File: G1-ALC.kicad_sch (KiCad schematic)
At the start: 91 parts, among them J101 Conn_01x03_Pin, J102 330 VAC In, J103 G1 connections, J104 105VAC in, J105 Conn_01x03_Pin, J107 Conn_01x05_Pin, J108 G2 Control board interconnect, Q101 TIP122, U101 LM7812_TO220, U102 LM324, U103 MCT5211M, U301 CNY17-4

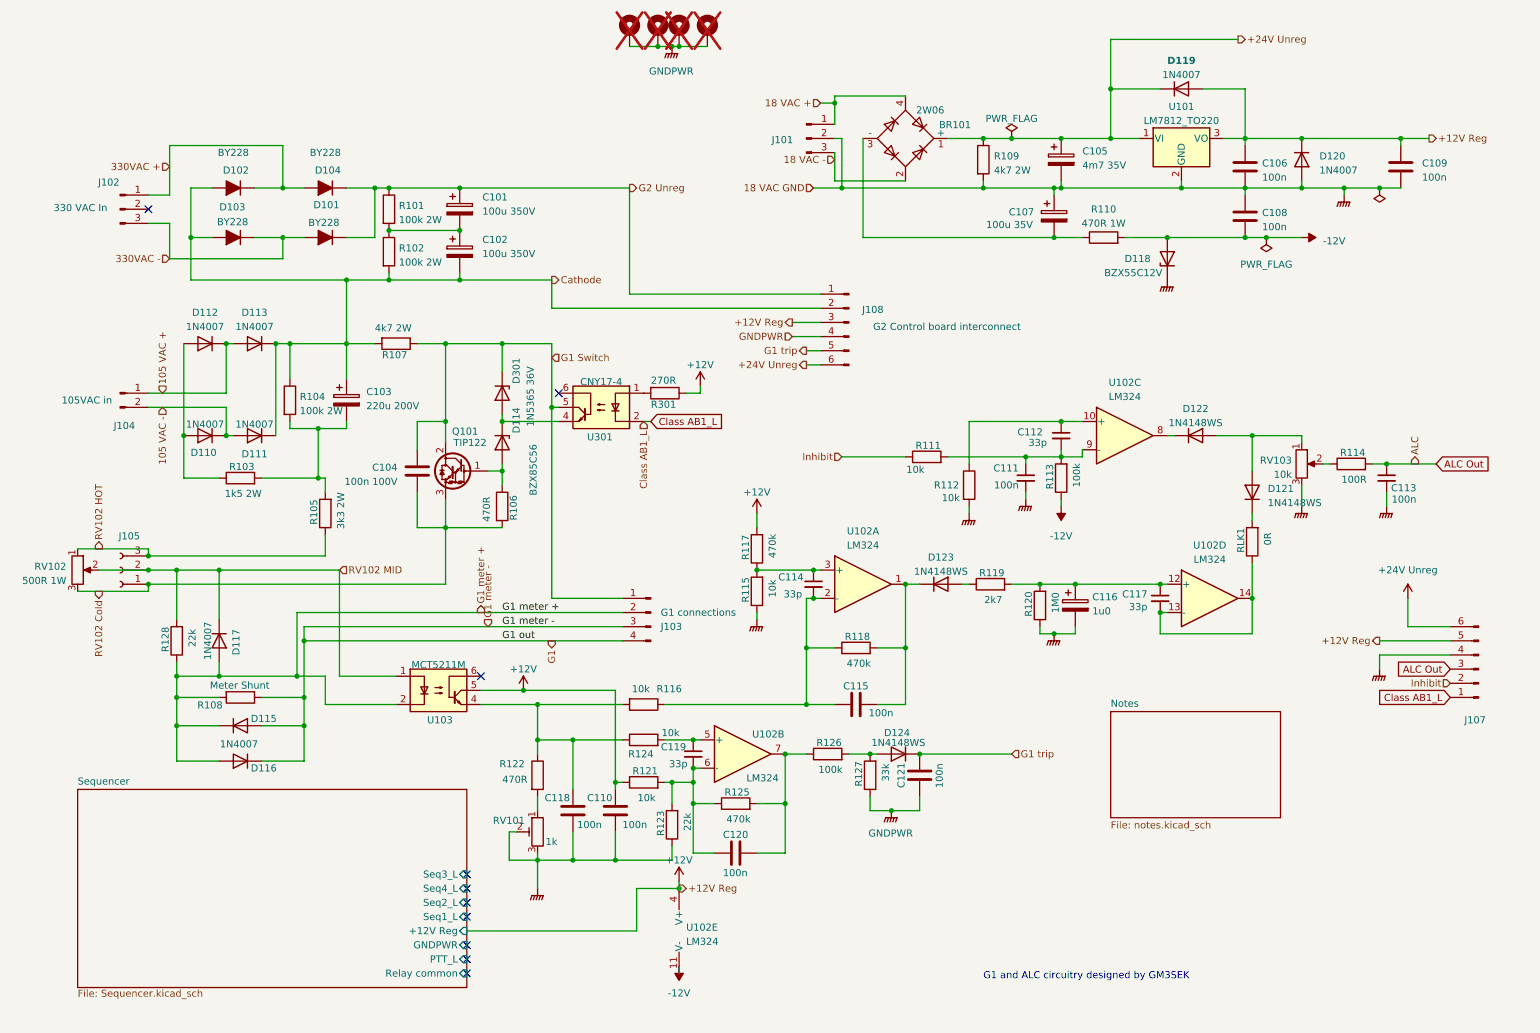
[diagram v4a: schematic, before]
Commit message: Cleanup schematic. No functional change.
Replaced global labels with hierarchical.
Consistent placement of references and values.
Values typed in a smaller font.
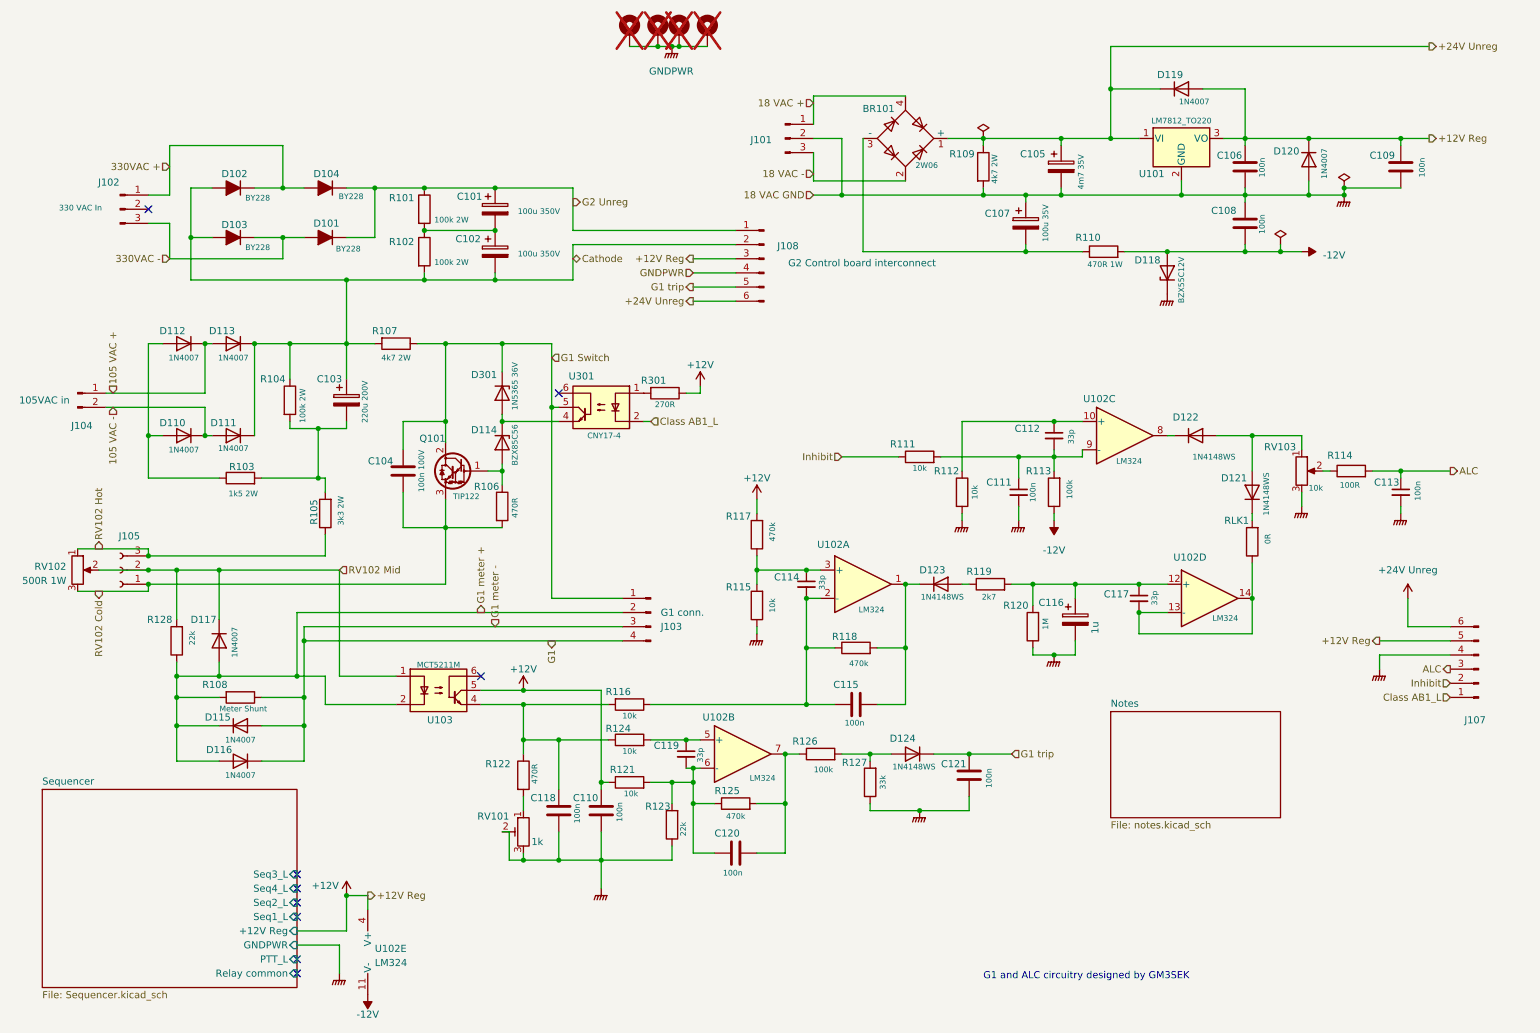
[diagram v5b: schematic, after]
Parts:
- C116: value 1u0 -> 1u
- J103: value G1 connections -> G1 conn.
- R120: value 1M0 -> 1M
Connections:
- net ALC Out renamed ALC
- net RV102 HOT renamed RV102 Hot
- net RV102 MID renamed RV102 Mid
- no-connect marks 10 -> 9
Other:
- moved on the sheet: C101, C102, C104, C105, C107, C108, C110, C111, C112, C113, C114, C116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

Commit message: Moved cold end of R115 to CLASS_AB1_L instead of GND. The intent is to turn off ALC in case we want to run the PA in class C.
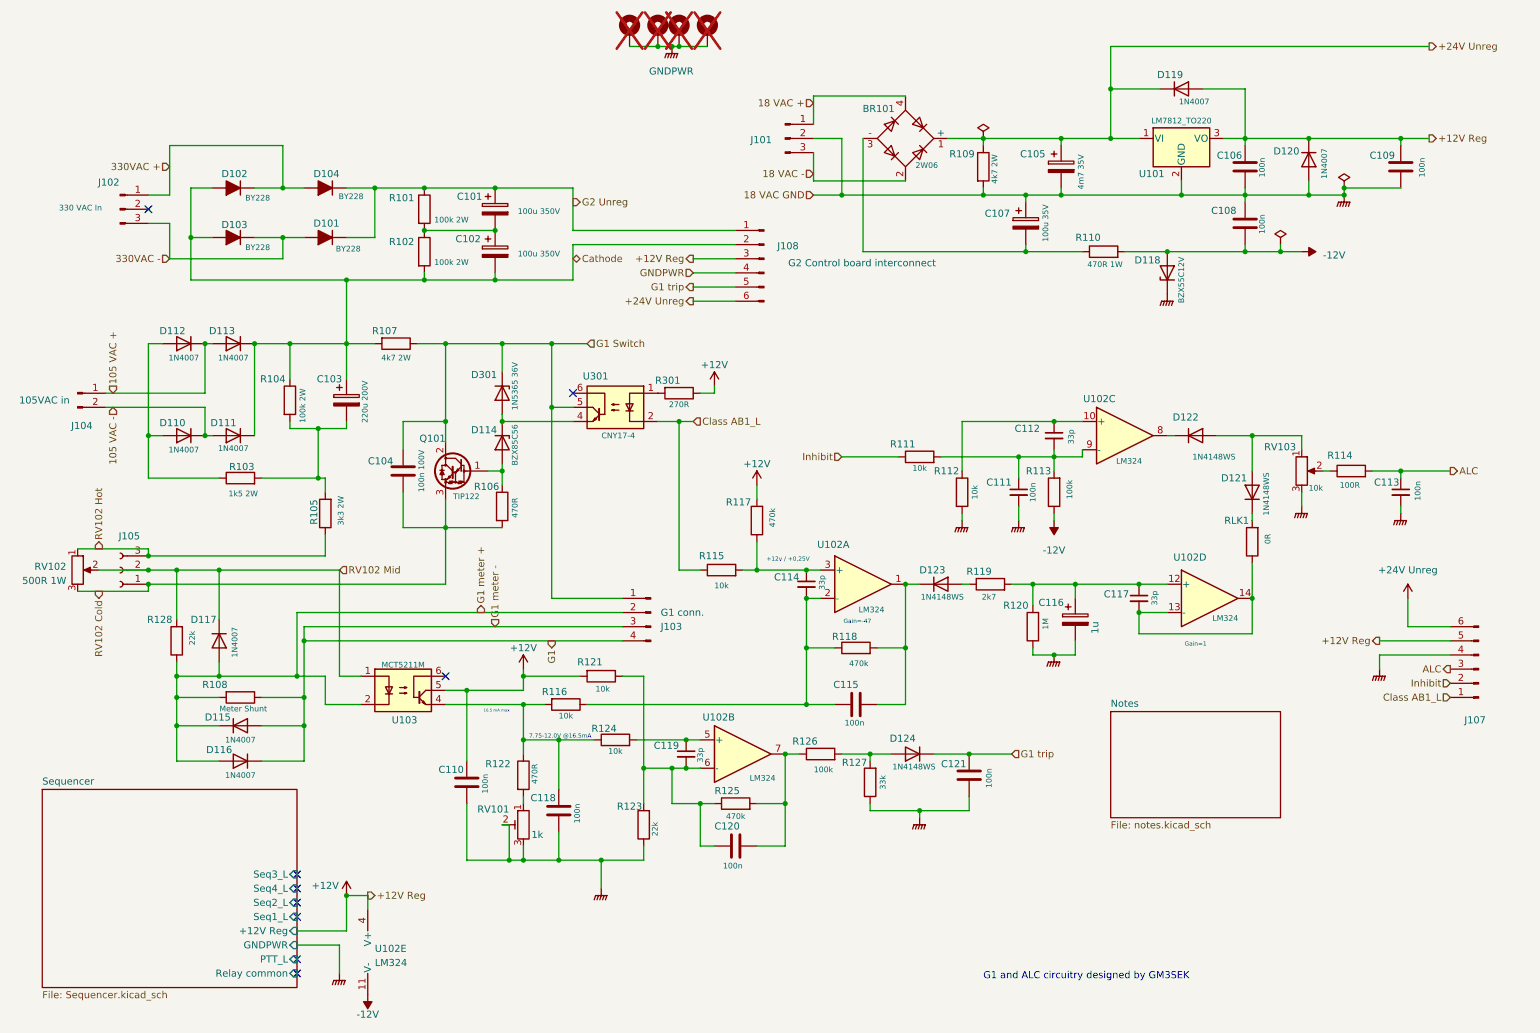
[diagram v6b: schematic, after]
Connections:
- net +12V: now also R121.2; no longer R121.1
- net Class AB1_L: now also R115.1
- net GNDPWR: no longer R115.1
- net at C119.2, C120.1, R123.2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: now also R121.1; no longer R121.2
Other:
- note added: "+12v / +0,25V"
- note added: "16.5 mA max"
- note added: "7.75-12.0V @16.5mA"
- note added: "Gain=-47"
- note added: "Gain=1"
- moved on the sheet: C110, C120, R115, R116, R117, R121, R123, R124, R301, RV101, U103, U301

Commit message: Updated format to KiCad 9. Included footprints etc.
Standardized PCB layers, updated property formatting, and adjusted net assignments. Added some DigiKey, Electrokit, and Mouser component part numbers.
Reduced font sizes for better readability and incorporated embedded font settings.
Removed the sequencer from the schematic which wasn't really meant to be there.
Revised and excluded drc and erc warnings and exclusions.
Included footprints into the project library that formerly was defined outside of the project.
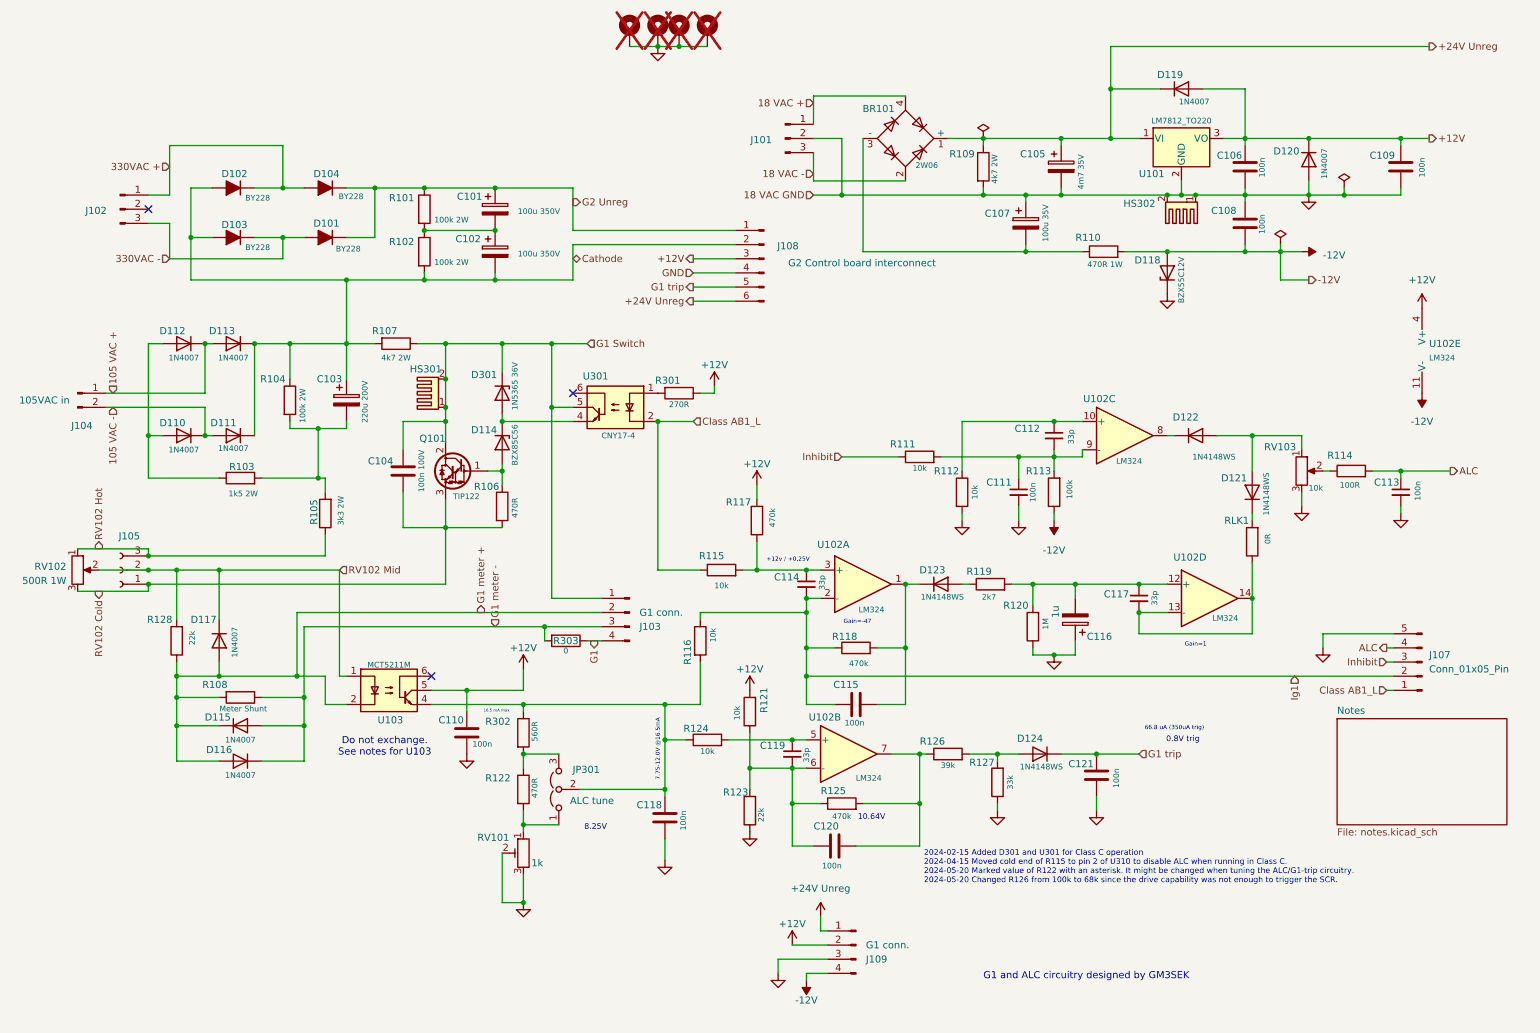
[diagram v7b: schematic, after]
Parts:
- removed J107: Conn_01x05_Pin, Connector_Phoenix_MSTB:PhoenixContact_MSTBVA_2,5_6-G-5,08_1x06_P5.08mm_Vertical, symbol Connector:Conn_01x06_Pin
- removed unit 5 of U102
- added HS301, HS302: Heatsink_Pad_2Pin, Project_library:6025DG_Cooler, symbol Mechanical:Heatsink_Pad_2Pin
- added J107: Conn_01x05_Pin, Connector_Phoenix_MSTB:PhoenixContact_MSTBVA_2,5_5-G-5,08_1x05_P5.08mm_Vertical, symbol Connector:Conn_01x05_Pin
- added J109: G1 conn., Connector_Phoenix_MSTB:PhoenixContact_MSTBVA_2,5_4-G-5,08_1x04_P5.08mm_Vertical, symbol Connector:Conn_01x04_Pin
- added JP301: ALC tune, Connector_PinHeader_2.54mm:PinHeader_1x03_P2.54mm_Vertical, symbol Jumper:Jumper_3_Open
- added R302: 560R, Resistor_SMD:R_1206_3216Metric, symbol Device:R
- added R303: 0, Jumper:SolderJumper-2_P1.3mm_Bridged2Bar_RoundedPad1.0x1.5mm, symbol Device:R
- BR101: Electrokit # (none) -> 40310051; Order # 40310051 -> (none); Supplier Electrokit -> (none)
- C101, C102: Electrokit # (none) -> 41004525; Order # 41004525 -> (none); Supplier Electrokit -> (none)
- C103: Electrokit # (none) -> 41019009; Order # 41019009 -> (none); Supplier Electrokit -> (none)
- C104: Electrokit # (none) -> 41015673; Order # 41015673 -> (none); Supplier Electrokit -> (none)
- C105: Electrokit # (none) -> 41016024; Order # 41016024 -> (none); Supplier Electrokit -> (none)
- C106, C108, C109, C110, C111, C113, C115, C118, C120, C121: Electrokit # (none) -> 40503054; Mouser # (none) -> 80-C1206C104M5R; Order # 40503054 -> (none); Supplier Electrokit -> (none)
- C107: Electrokit # (none) -> 41019011; Order # 41019011 -> (none); Supplier Electrokit -> (none)
- C112, C114, C117, C119: Electrokit # (none) -> 40502045; Mouser # (none) -> 791-0805N330K250CT; Order # 40502045 -> (none); Supplier Electrokit -> (none)
- C116: Electrokit # (none) -> 40503060; Mouser # (none) -> 187-CL31B105KAHNFNE; Order # 40503060 -> (none); Supplier Electrokit -> (none)
- D101, D102, D103, D104: footprint Diode_THT_AKL:D_SOD-64_P15.24mm_big_holes_Horizontal -> Project_library:D_SOD-64_P15.24mm_big_holes_Horizontal; Electrokit # (none) -> 40311228; Order # 40311228 -> (none); Supplier Electrokit -> (none)
- D110, D111, D112, D113, D115, D116, D117, D119, D120: Electrokit # (none) -> 40310007; Order # 40310007 -> (none); Supplier Electrokit -> (none)
- D114, D301: Electrokit # (none) -> 41020328; Order # 41020328 -> (none); Supplier Electrokit -> (none)
- D118: Electrokit # (none) -> 40310033; Order # 40310033 -> (none); Supplier Electrokit -> (none)
- D121, D122, D123, D124: Electrokit # (none) -> 41011670; Mouser # (none) -> 637-1N4148WS; Order # 41011670 -> (none); Supplier Electrokit -> (none)
- H101: renamed from H105; Supplier Elecrow -> (none)
- H102: renamed from H101; Supplier Elecrow -> (none)
- H103: renamed from H102; Supplier Elecrow -> (none)
- H104: renamed from H103; Supplier Elecrow -> (none)
- J101, J105: Electrokit # (none) -> 40210022; Order # 40210022 -> (none); Supplier Electrokit -> (none)
- J102: value 330 VAC In -> 330VAC; Electrokit # (none) -> 40210022; Order # 40210022 -> (none); Supplier Electrokit -> (none)
- J103: Electrokit # (none) -> 41017486; Order # 41017486 -> (none); Supplier Electrokit -> (none)
- J104: Electrokit # (none) -> 40210021; Order # 40210021 -> (none); Supplier Electrokit -> (none)
- J108: Electrokit # (none) -> 41017488; Order # 41017488 -> (none); Supplier Electrokit -> (none)
- Q101: footprint Package_TO_SOT_THT:TO-220-3_Vertical_Cooler -> Package_TO_SOT_THT:TO-220-3_Vertical; Electrokit # (none) -> 40320122; Order # 40320122 -> (none); Supplier Electrokit -> (none)
- R101, R102, R104: Electrokit # (none) -> 41011683; Order # 41011683 -> (none); Supplier Electrokit -> (none)
- R103: Electrokit # (none) -> 41011674; Order # 41011674 -> (none); Supplier Electrokit -> (none)
- R105: Electrokit # (none) -> 41011677; Order # 41011677 -> (none); Supplier Electrokit -> (none)
- R106: Electrokit # (none) -> 40818247; Mouser # (none) -> 603-AF1206JR-07470RL; Order # 40818247 -> (none); Supplier Electrokit -> (none)
- R107, R109: Electrokit # (none) -> 41011678; Order # 41011678 -> (none); Supplier Electrokit -> (none)
- R108: Electrokit # (none) -> 40818315; Order # 40818315 -> (none); Supplier Electrokit -> (none)
- R110: Electrokit # (none) -> 40812020; Order # 40812020 -> (none); Supplier Electrokit -> (none)
- R111, R112, R115, R116, R121, R124: Electrokit # (none) -> 40818410; Mouser # (none) -> 603-AC1206FR-0710KL; Order # 40818410 -> (none); Supplier Electrokit -> (none)
- R113: Electrokit # (none) -> 40818510; Mouser # (none) -> 708-RMCF1206JG100K; Order # 40818510 -> (none); Supplier Electrokit -> (none)
- R114: Electrokit # (none) -> 40818210; Mouser # (none) -> 603-RC1206JR-13100RL; Order # 40818210 -> (none); Supplier Electrokit -> (none)
- R117, R118, R125: Electrokit # (none) -> 40818547; Mouser # (none) -> 652-CR1206JW-474ELF; Order # 40818547 -> (none); Supplier Electrokit -> (none)
- R119: Electrokit # (none) -> 40818327; Mouser # (none) -> 652-CR1206FX-2701ELF; Order # 40818327 -> (none); Supplier Electrokit -> (none)
- R120: Electrokit # (none) -> 40818610; Mouser # (none) -> 279-CRGP1206F1M0; Order # 40818610 -> (none); Supplier Electrokit -> (none)
- R122: Order # 40818247 -> (none); Supplier Electrokit -> (none)
- R123, R128: Electrokit # (none) -> 40818315; Mouser # (none) -> 71-CRCW1206-22K-E3; Order # 40818315 -> (none); Supplier Electrokit -> (none)
- R126: value 100k -> 39k; Electrokit # (none) -> 40818510; Mouser # (none) -> 667-ERJ-P08J683V; Order # 40818510 -> (none); Supplier Electrokit -> (none)
- R127: Electrokit # (none) -> 40818433; Mouser # (none) -> 652-CR1206FX-3302ELF; Order # 40818433 -> (none); Supplier Electrokit -> (none)
- R301: Electrokit # (none) -> 40818227; Order # 40818227 -> (none); Supplier Electrokit -> (none)
- RLK1: Electrokit # (none) -> 40818433; Order # 40818433 -> (none); Supplier Electrokit -> (none)
- RV101: Electrokit # (none) -> 33860102; Order # 33860102 -> (none); Supplier Electrokit -> (none)
- RV102: Mouser # (none) -> 3109605596; Order # 3109605596 -> (none); Supplier Mouser -> (none)
- RV103: Electrokit # (none) -> 33860103; Order # 33860103 -> (none); Supplier Electrokit -> (none)
- U101: footprint Package_TO_SOT_THT:TO-220-3_Vertical_Cooler -> Package_TO_SOT_THT:TO-220-3_Vertical; Electrokit # (none) -> 41009663; Order # 41009663 -> (none); Supplier Electrokit -> (none)
- U102: Electrokit # (none) -> 40350324; Mouser # (none) -> 863-LM324DR2G; Order # 40350324 -> (none); Supplier Electrokit -> (none)
- U103: DigiKey # (none) -> MCT5211M-ND; Notes This component is crucial. It cannot simply be exchanged for any other optocoupler because its sensititity to low LED current is needed. -> This component is crucial. It cannot simply be exchanged for any other optocoupler because its sensititity to low grid current is needed.; Order # MCT5211M-ND -> (none); Supplier DigiKey -> (none)
- U301: DigiKey # (none) -> 751-1268-5-ND; Order # 751-1268-5-ND -> (none); Supplier DigiKey -> (none)
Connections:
- net +12V: now also U102.4 (V+), J109.2 (Pin_2)
- net +24V Unreg: now also J109.1 (Pin_1)
- net -12V: now also U102.11 (V-), J109.4 (Pin_4)
- net ALC: now also J107.4 (Pin_4)
- net Class AB1_L: now also J107.1 (Pin_1)
- net G1: now also R303.1; no longer D115.2 (A), D116.1 (K), J103.3 (Pin_3), R108.1
- net G1 Switch: now also HS301.1, HS301.2
- net Inhibit: now also J107.3 (Pin_3)
- net at C118.1, R116.2, R124.1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: now also JP301.2 (C), R302.1; no longer R122.1
- net at C117.1, R119.2, R120.2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: now also C116.2; no longer C116.1
- net Ig1: now reaches C114.2, C115.1, R116.1, R118.1, U102.2 (-)
- net Ig1: now also J107.2 (Pin_2)
- net at R122.2, RV101.1: now also JP301.1 (A)
- net GNDPWR renamed GND
- net GND: now also C116.1, HS302.1, HS302.2, J107.5 (Pin_5), J109.3 (Pin_3); no longer C116.2
- new net: JP301.3 (B), R122.1, R302.2
- new net G1 meter -: D115.2 (A), D116.1 (K), J103.3 (Pin_3), R108.1, R303.2
- no-connect marks 9 -> 3
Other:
- removed sheet Sequencer
- note added: "0.8V trig"
- note added: "10.64V"
- note added: "2024-02-15 Added D301 and U301 for Class C operation 2024-04-15 Moved cold end of R115 to pin 2 of U310 to disable ALC when running in Class C. 2024-05-20 Marked value of R122 with an asterisk. It might be changed when tuning the ALC/G1-trip circuitry. 2024-05-20 Changed R126 from 100k to 68k since the drive capability was not enough to trigger the SCR."
- note added: "66.8 uA (350uA trig)"
- note added: "8.25V"
- note added: "Do not exchange. See notes for U103"
- moved on the sheet: C110, C116, C118, C119, C120, C121, D124, J103, R116, R121, R122, R123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
